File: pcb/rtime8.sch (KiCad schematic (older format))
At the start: 14 parts, among them J2 ICSP, U5 PIC24FJ32GA004-I/PT, Y1 32768

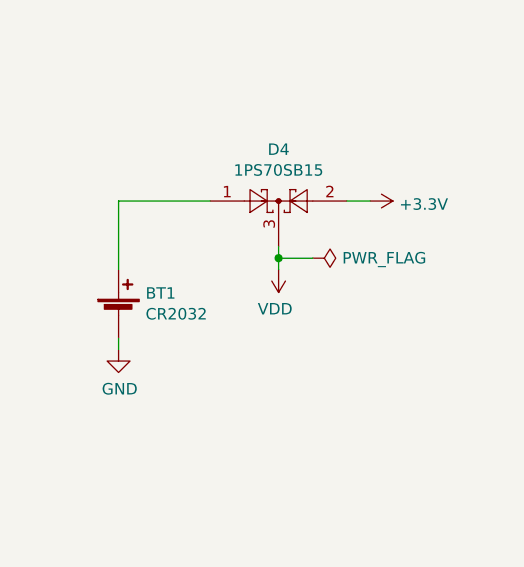
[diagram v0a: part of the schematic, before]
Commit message: PCB: Add connector for measuring deep sleep current
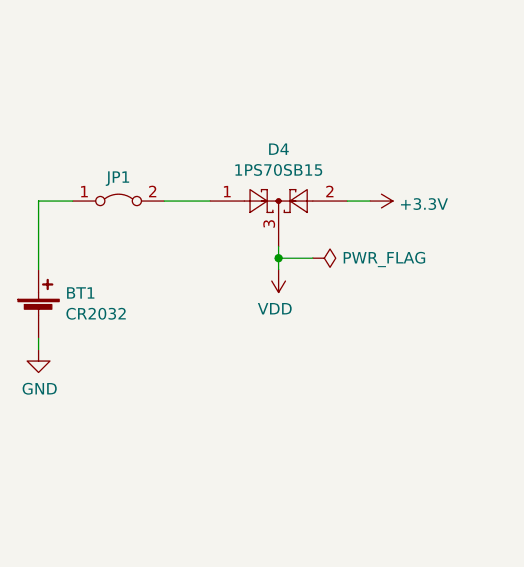
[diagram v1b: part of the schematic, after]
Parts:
- added JP1: Jumper_2_Bridged, Connector_PinHeader_2.54mm:PinHeader_1x02_P2.54mm_Vertical, symbol Jumper:Jumper_2_Bridged
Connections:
- net at BT1.1 (+): now also JP1.1 (A); no longer D4.1
- new net: D4.1, JP1.2 (B)
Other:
- moved on the sheet: BT1
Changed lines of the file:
@@
 L Device:Battery_Cell BT1
 U 1 1 6102C16A
-P 3350 3700
-F 0 "BT1" H 3468 3796 50  0000 L CNN
-F 1 "CR2032" H 3468 3705 50  0000 L CNN
-F 2 "Miscellaneous:BatteryHolder_Connfly_DS1092-10" V 3350 3760 50  0001 C CNN
-F 3 "~" V 3350 3760 50  0001 C CNN
-	1    3350 3700
+P 3000 3700
+F 0 "BT1" H 3118 3796 50  0000 L CNN
+F 1 "CR2032" H 3118 3705 50  0000 L CNN
+F 2 "Miscellaneous:BatteryHolder_Connfly_DS1092-10" V 3000 3760 50  0001 C CNN
+F 3 "~" V 3000 3760 50  0001 C CNN
+	1    3000 3700
 	1    0    0    -1
 $EndComp
@@
 L power:GND #PWR0118
 U 1 1 6102C63F
-P 3350 3850
-F 0 "#PWR0118" H 3350 3600 50  0001 C CNN
-F 1 "GND" H 3355 3677 50  0000 C CNN
-F 2 "" H 3350 3850 50  0001 C CNN
-F 3 "" H 3350 3850 50  0001 C CNN
-	1    3350 3850
+P 3000 3850
+F 0 "#PWR0118" H 3000 3600 50  0001 C CNN
+F 1 "GND" H 3005 3677 50  0000 C CNN
+F 2 "" H 3000 3850 50  0001 C CNN
+F 3 "" H 3000 3850 50  0001 C CNN
+	1    3000 3850
 	1    0    0    -1
 $EndComp
 Wire Wire Line
-	3350 3850 3350 3800
+	3000 3850 3000 3800
 Wire Wire Line
 	3650 4900 3600 4900
@@
 $EndComp
 Wire Wire Line
-	3350 3500 3350 3200
-Wire Wire Line
-	3350 3200 3750 3200
+	3000 3500 3000 3200
 $Comp
 L power:VDD #PWR0119
@@
 	1    0    0    1
 $EndComp
+$Comp
+L Jumper:Jumper_2_Bridged JP1
+U 1 1 61224A7B
+P 3350 3200
+F 0 "JP1" H 3350 3303 50  0000 C CNN
+F 1 "Jumper_2_Bridged" H 3350 3304 50  0001 C CNN
+F 2 "Connector_PinHeader_2.54mm:PinHeader_1x02_P2.54mm_Vertical" H 3350 3200 50  0001 C CNN
+F 3 "~" H 3350 3200 50  0001 C CNN
+	1    3350 3200
+	1    0    0    -1
+$EndComp
+Wire Wire Line
+	3000 3200 3150 3200
+Wire Wire Line
+	3550 3200 3750 3200
 $EndSCHEMATC

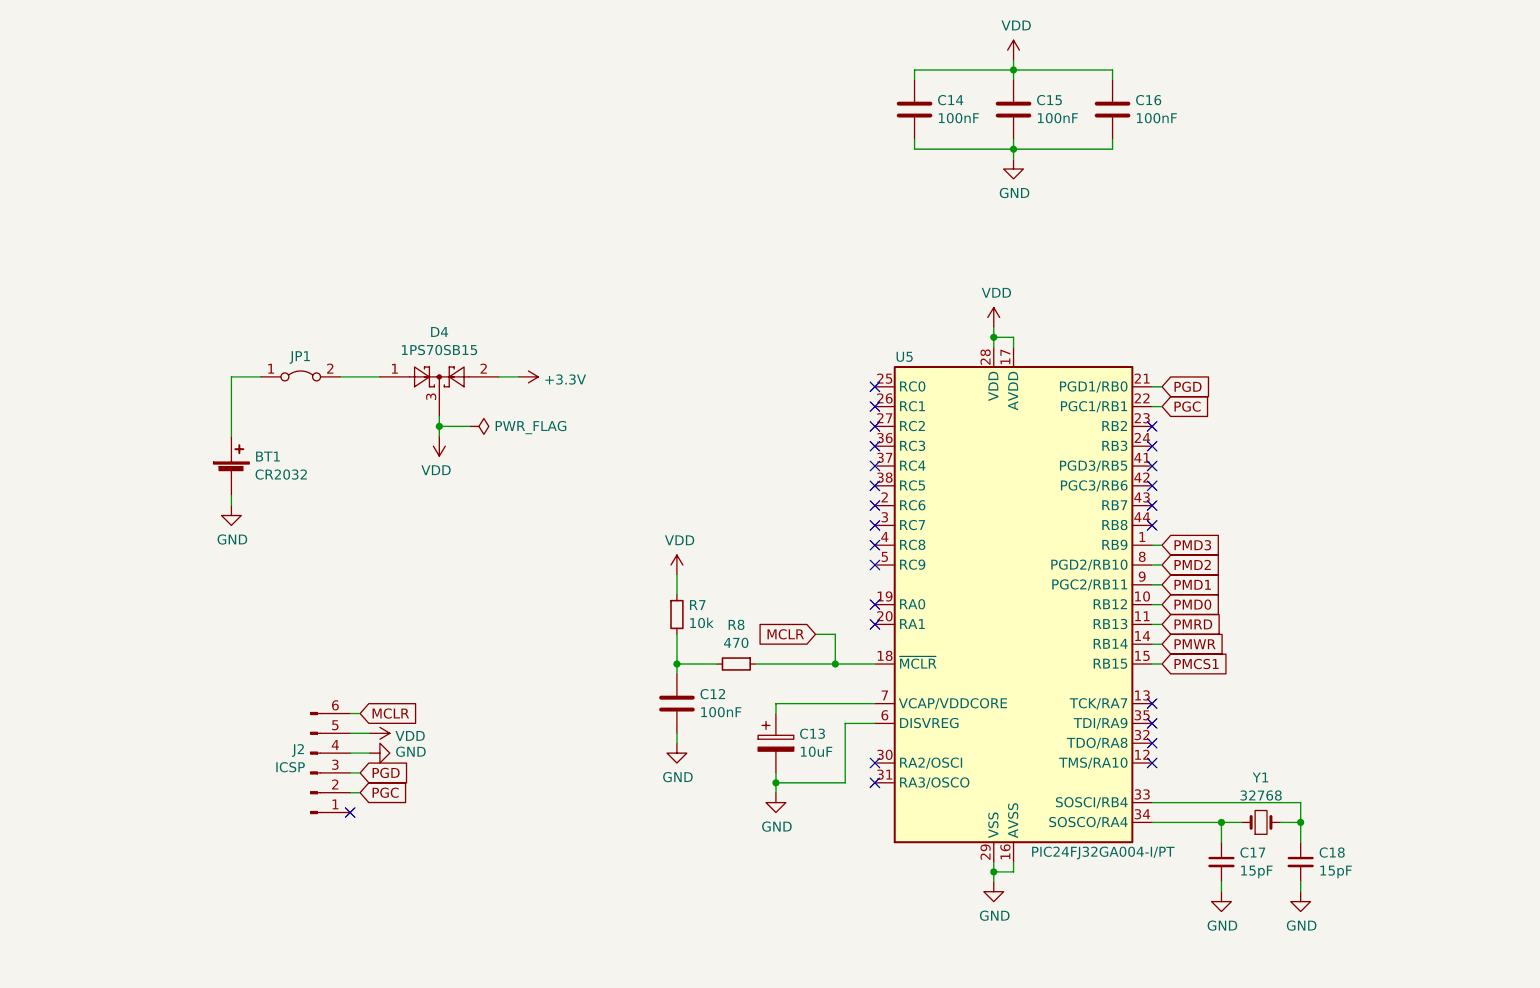
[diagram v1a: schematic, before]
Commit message: PCB: Add test connector
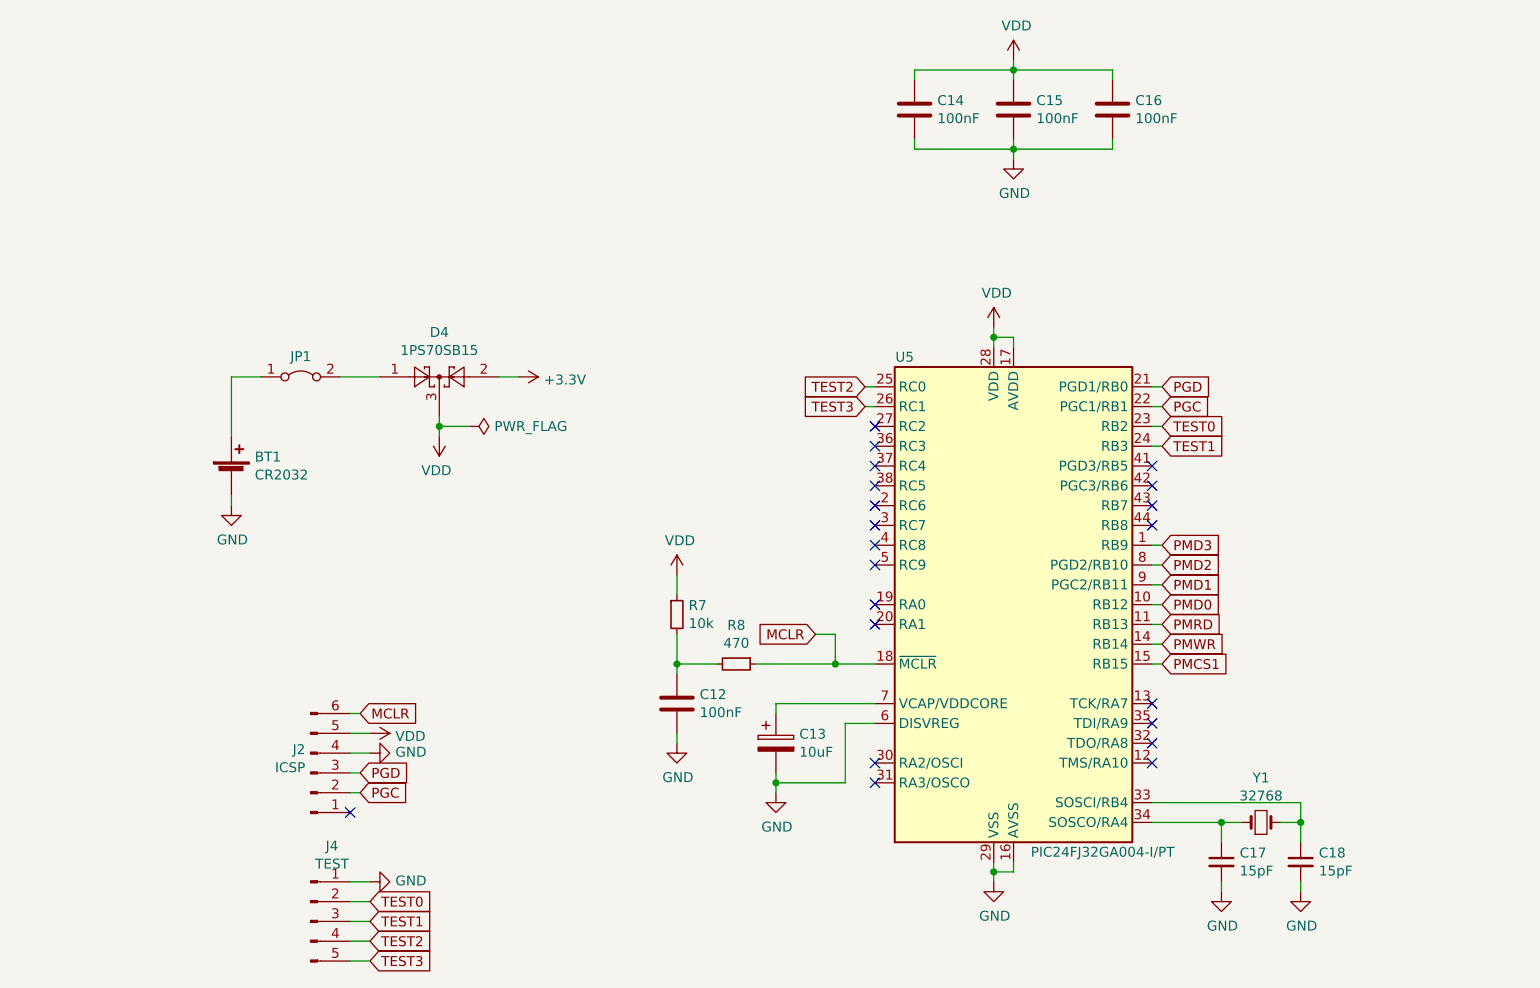
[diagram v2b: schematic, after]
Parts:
- added J4: TEST, Connector_PinHeader_2.54mm:PinHeader_1x05_P2.54mm_Vertical, symbol Connector:Conn_01x05_Male
- added TEST0: GND, symbol power:GND
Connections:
- net GND: now also J4.1 (Pin_1), TEST0.1 (GND)
- net TEST0: now reaches U5.23 (RB2)
- net TEST0: now also J4.2 (Pin_2)
- net TEST1: now reaches U5.24 (RB3)
- net TEST1: now also J4.3 (Pin_3)
- net TEST2: now reaches U5.25 (RC0)
- net TEST2: now also J4.4 (Pin_4)
- net TEST3: now reaches U5.26 (RC1)
- net TEST3: now also J4.5 (Pin_5)
- no-connect marks 25 -> 21
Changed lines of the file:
@@
 NoConn ~ 6250 3550
 NoConn ~ 6250 3450
-NoConn ~ 6250 3350
-NoConn ~ 6250 3250
-NoConn ~ 7650 3450
-NoConn ~ 7650 3550
 NoConn ~ 7650 3650
 NoConn ~ 7650 3750
@@
 Wire Wire Line
 	3550 3200 3750 3200
+$Comp
+L Connector:Conn_01x05_Male J4
+U 1 1 61241826
+P 3400 5950
+F 0 "J4" H 3508 6331 50  0000 C CNN
+F 1 "TEST" H 3508 6240 50  0000 C CNN
+F 2 "Connector_PinHeader_2.54mm:PinHeader_1x05_P2.54mm_Vertical" H 3400 5950 50  0001 C CNN
+F 3 "~" H 3400 5950 50  0001 C CNN
+	1    3400 5950
+	1    0    0    -1
+$EndComp
+$Comp
+L power:GND TEST0
+U 1 1 612443C8
+P 3700 5750
+F 0 "TEST0" H 3700 5500 50  0001 C CNN
+F 1 "GND" V 3705 5622 50  0000 R CNN
+F 2 "" H 3700 5750 50  0001 C CNN
+F 3 "" H 3700 5750 50  0001 C CNN
+	1    3700 5750
+	0    -1   -1   0
+$EndComp
+Wire Wire Line
+	3700 5750 3600 5750
+Text GLabel 3700 5850 2    50   Input ~ 0
+TEST0
+Text GLabel 3700 5950 2    50   Input ~ 0
+TEST1
+Text GLabel 3700 6050 2    50   Input ~ 0
+TEST2
+Text GLabel 3700 6150 2    50   Input ~ 0
+TEST3
+Wire Wire Line
+	3600 6150 3700 6150
+Wire Wire Line
+	3700 6050 3600 6050
+Wire Wire Line
+	3600 5950 3700 5950
+Wire Wire Line
+	3600 5850 3700 5850
+Text GLabel 7700 3450 2    50   Input ~ 0
+TEST0
+Text GLabel 7700 3550 2    50   Input ~ 0
+TEST1
+Text GLabel 6200 3250 0    50   Input ~ 0
+TEST2
+Text GLabel 6200 3350 0    50   Input ~ 0
+TEST3
+Wire Wire Line
+	6200 3250 6250 3250
+Wire Wire Line
+	6250 3350 6200 3350
+Wire Wire Line
+	7700 3450 7650 3450
+Wire Wire Line
+	7650 3550 7700 3550
 $EndSCHEMATC

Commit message: PCB: Add quartz crystal description
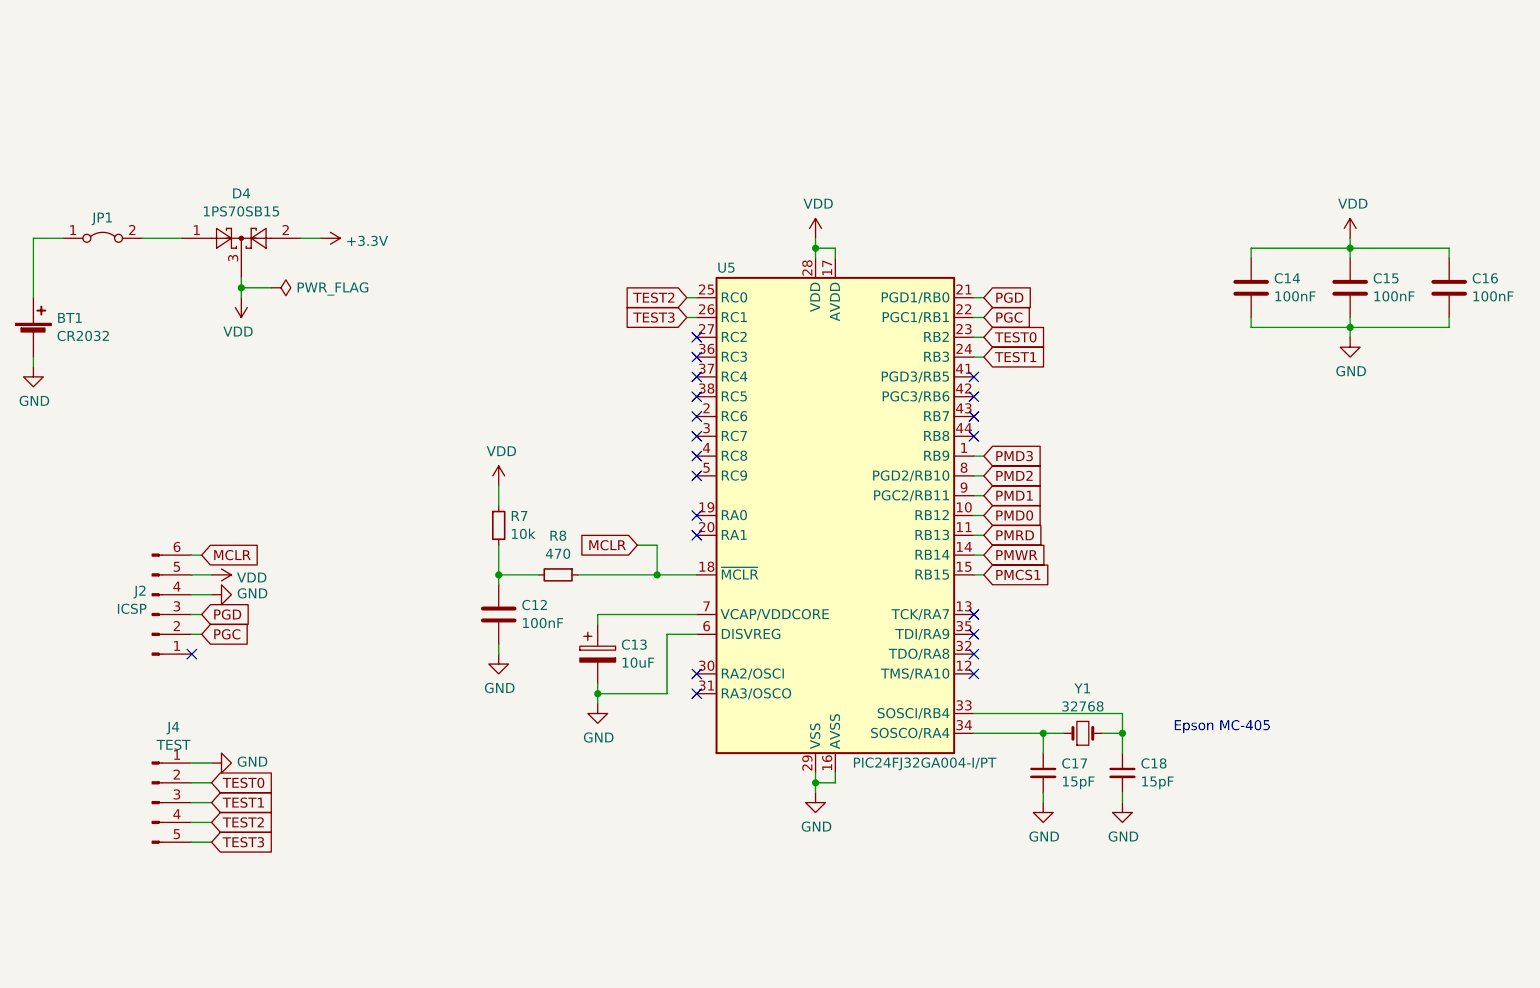
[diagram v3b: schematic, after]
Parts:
- removed TEST0: GND, symbol power:GND
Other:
- note added: "Epson MC-405"
- moved on the sheet: BT1, C12, C13, C14, C15, C16, C17, C18, D4, J2, J4, JP1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

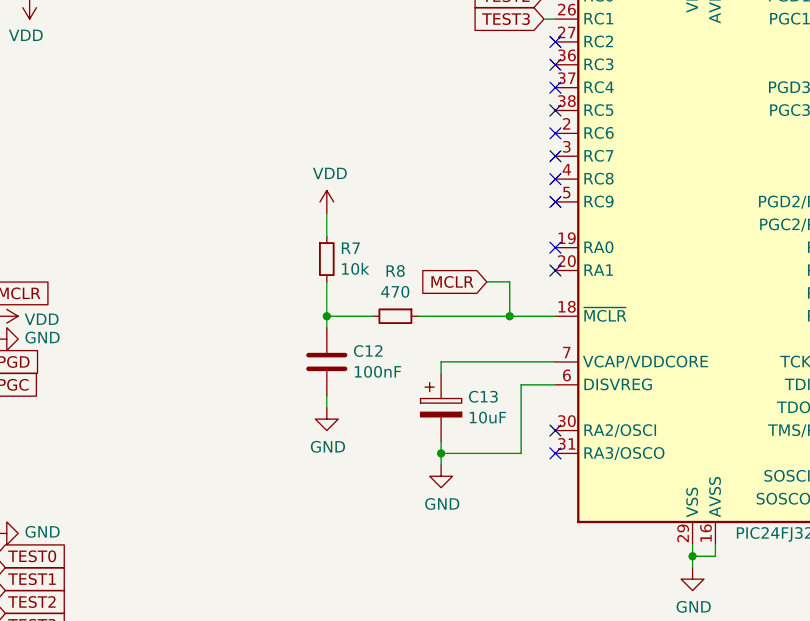
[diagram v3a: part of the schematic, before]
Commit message: Tweak connections between PLD and uC
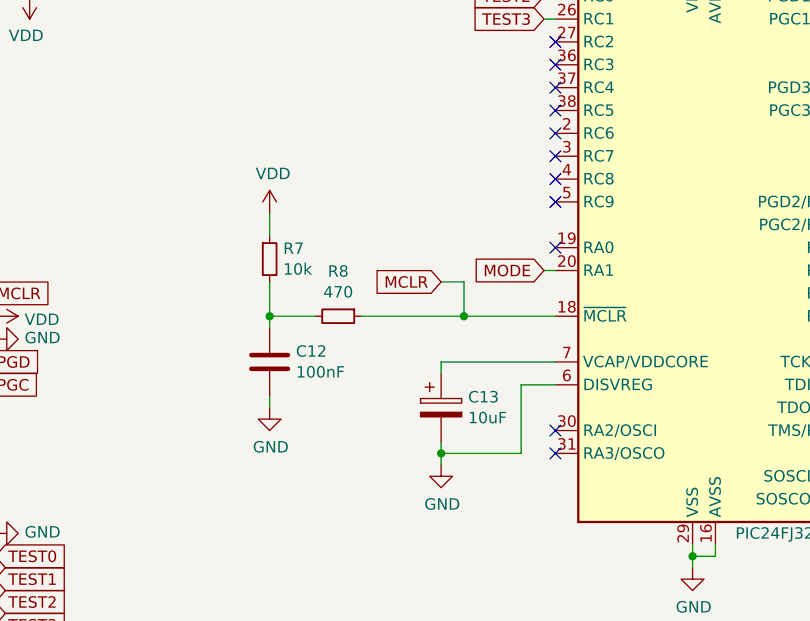
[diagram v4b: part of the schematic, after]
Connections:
- net MODE: now reaches U5.20 (RA1)
- no-connect marks 21 -> 20
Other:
- moved on the sheet: C12, R7, R8
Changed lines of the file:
@@
 Text GLabel 2850 4100 2    50   Input ~ 0
 MCLR
-Text GLabel 5050 4050 0    50   Input ~ 0
+Text GLabel 4850 4050 0    50   Input ~ 0
 MCLR
 $Comp
 L Device:R_Small R7
 U 1 1 60FE5D97
-P 4350 3950
-F 0 "R7" H 4409 3996 50  0000 L CNN
-F 1 "10k" H 4409 3905 50  0000 L CNN
-F 2 "Resistor_SMD:R_0805_2012Metric_Pad1.20x1.40mm_HandSolder" H 4350 3950 50  0001 C CNN
-F 3 "~" H 4350 3950 50  0001 C CNN
-	1    4350 3950
+P 4100 3950
+F 0 "R7" H 4159 3996 50  0000 L CNN
+F 1 "10k" H 4159 3905 50  0000 L CNN
+F 2 "Resistor_SMD:R_0805_2012Metric_Pad1.20x1.40mm_HandSolder" H 4100 3950 50  0001 C CNN
+F 3 "~" H 4100 3950 50  0001 C CNN
+	1    4100 3950
 	1    0    0    -1
 $EndComp
@@
 L Device:R_Small R8
 U 1 1 60FE701A
-P 4650 4200
-F 0 "R8" V 4454 4200 50  0000 C CNN
-F 1 "470" V 4545 4200 50  0000 C CNN
-F 2 "Resistor_SMD:R_0805_2012Metric_Pad1.20x1.40mm_HandSolder" H 4650 4200 50  0001 C CNN
-F 3 "~" H 4650 4200 50  0001 C CNN
-	1    4650 4200
+P 4400 4200
+F 0 "R8" V 4204 4200 50  0000 C CNN
+F 1 "470" V 4295 4200 50  0000 C CNN
+F 2 "Resistor_SMD:R_0805_2012Metric_Pad1.20x1.40mm_HandSolder" H 4400 4200 50  0001 C CNN
+F 3 "~" H 4400 4200 50  0001 C CNN
+	1    4400 4200
 	0    1    1    0
 $EndComp
@@
 L Device:C C12
 U 1 1 60FE7F0C
-P 4350 4400
-F 0 "C12" H 4465 4446 50  0000 L CNN
-F 1 "100nF" H 4465 4355 50  0000 L CNN
-F 2 "Capacitor_SMD:C_0805_2012Metric_Pad1.18x1.45mm_HandSolder" H 4388 4250 50  0001 C CNN
-F 3 "~" H 4350 4400 50  0001 C CNN
-	1    4350 4400
+P 4100 4400
+F 0 "C12" H 4215 4446 50  0000 L CNN
+F 1 "100nF" H 4215 4355 50  0000 L CNN
+F 2 "Capacitor_SMD:C_0805_2012Metric_Pad1.18x1.45mm_HandSolder" H 4138 4250 50  0001 C CNN
+F 3 "~" H 4100 4400 50  0001 C CNN
+	1    4100 4400
 	1    0    0    -1
 $EndComp
@@
 L power:VDD #PWR06
 U 1 1 60FECB3D
-P 4350 3750
-F 0 "#PWR06" H 4350 3600 50  0001 C CNN
-F 1 "VDD" H 4365 3923 50  0000 C CNN
-F 2 "" H 4350 3750 50  0001 C CNN
-F 3 "" H 4350 3750 50  0001 C CNN
-	1    4350 3750
-	1    0    0    -1
-$EndComp
-Wire Wire Line
-	4350 3750 4350 3850
-Wire Wire Line
-	4350 4050 4350 4200
+P 4100 3750
+F 0 "#PWR06" H 4100 3600 50  0001 C CNN
+F 1 "VDD" H 4115 3923 50  0000 C CNN
+F 2 "" H 4100 3750 50  0001 C CNN
+F 3 "" H 4100 3750 50  0001 C CNN
+	1    4100 3750
+	1    0    0    -1
+$EndComp
+Wire Wire Line
+	4100 3750 4100 3850
+Wire Wire Line
+	4100 4050 4100 4200
 $Comp
 L power:GND #PWR07
 U 1 1 60FEE618
-P 4350 4600
-F 0 "#PWR07" H 4350 4350 50  0001 C CNN
-F 1 "GND" H 4355 4427 50  0000 C CNN
-F 2 "" H 4350 4600 50  0001 C CNN
-F 3 "" H 4350 4600 50  0001 C CNN
-	1    4350 4600
-	1    0    0    -1
-$EndComp
-Wire Wire Line
-	4350 4600 4350 4550
-Wire Wire Line
-	4350 4200 4550 4200
-Connection ~ 4350 4200
-Wire Wire Line
-	4350 4200 4350 4250
-Wire Wire Line
-	4750 4200 5150 4200
-Wire Wire Line
-	5050 4050 5150 4050
-Wire Wire Line
-	5150 4050 5150 4200
-Connection ~ 5150 4200
-Wire Wire Line
-	5150 4200 5350 4200
+P 4100 4600
+F 0 "#PWR07" H 4100 4350 50  0001 C CNN
+F 1 "GND" H 4105 4427 50  0000 C CNN
+F 2 "" H 4100 4600 50  0001 C CNN
+F 3 "" H 4100 4600 50  0001 C CNN
+	1    4100 4600
+	1    0    0    -1
+$EndComp
+Wire Wire Line
+	4100 4600 4100 4550
+Wire Wire Line
+	4100 4200 4300 4200
+Connection ~ 4100 4200
+Wire Wire Line
+	4100 4200 4100 4250
+Wire Wire Line
+	4500 4200 4950 4200
+Wire Wire Line
+	4850 4050 4950 4050
+Wire Wire Line
+	4950 4050 4950 4200
+Connection ~ 4950 4200
+Wire Wire Line
+	4950 4200 5350 4200
 Text GLabel 2850 4400 2    50   Input ~ 0
 PGD
@@
 NoConn ~ 5350 4800
 NoConn ~ 5350 4700
-NoConn ~ 5350 4000
 NoConn ~ 5350 3900
 NoConn ~ 5350 3700
@@
 Text Notes 8250 5000 2    50   ~ 0
 Epson MC-405
+Text GLabel 5300 4000 0    50   Input ~ 0
+MODE
+Wire Wire Line
+	5300 4000 5350 4000
 $EndSCHEMATC
